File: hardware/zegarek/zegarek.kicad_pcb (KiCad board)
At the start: 4 copper layers, 100 x 100 mm, 106 parts, among them J1 Barrel_Jack_MountingPin, J2 Conn_01x02, J3 Conn_01x02, J4 Conn_01x04, M1 74141DIP16, M2 74141DIP16, M3 74141DIP16, M4 74141DIP16, Q1 IRF740, SW1 SW_Push, SW2 SW_Push, SW3 SW_Push, SW4 SW_Push, U1 DI78L3.3UAB, U2 MC34063AD, U3 L7805ACV, U4 STM32F091RCTx, U5 SN74LVC8T245, U6 SN74LVC8T245, Y1 32.768kHz

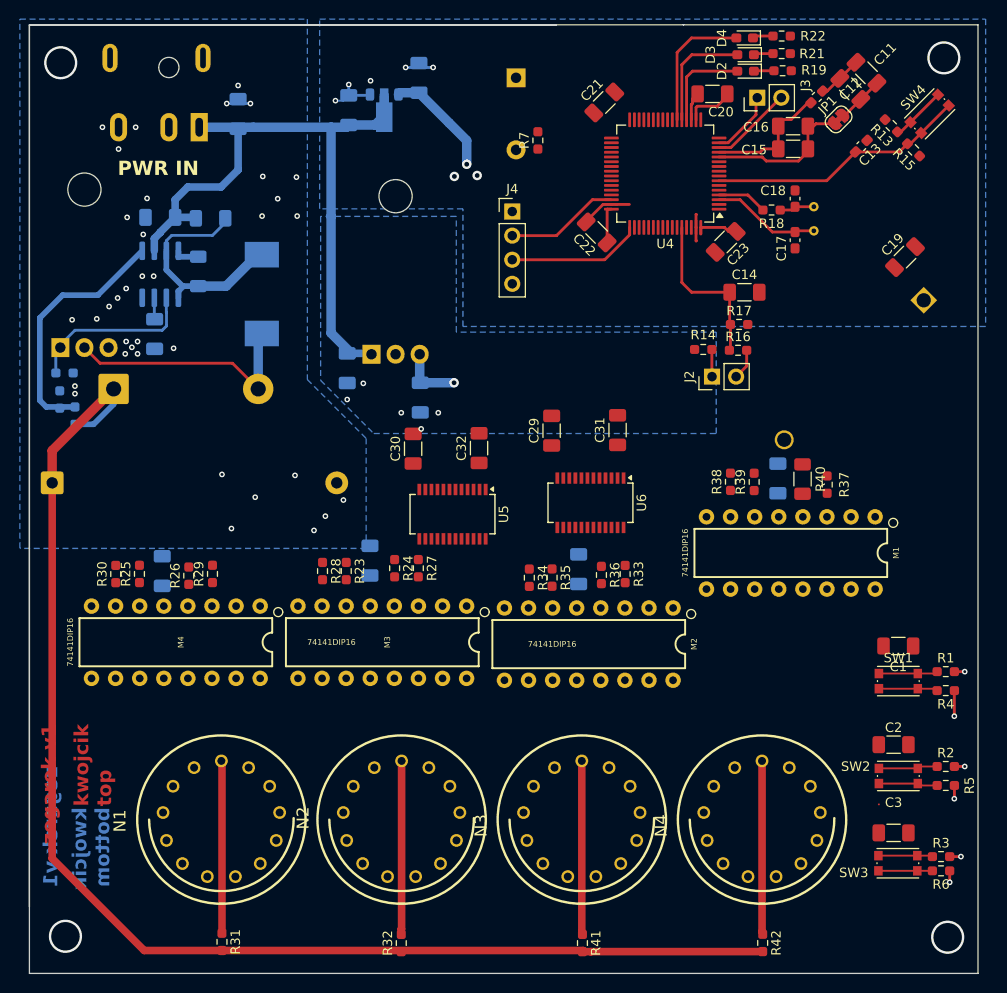
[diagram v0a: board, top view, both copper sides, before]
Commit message: tracing lamps
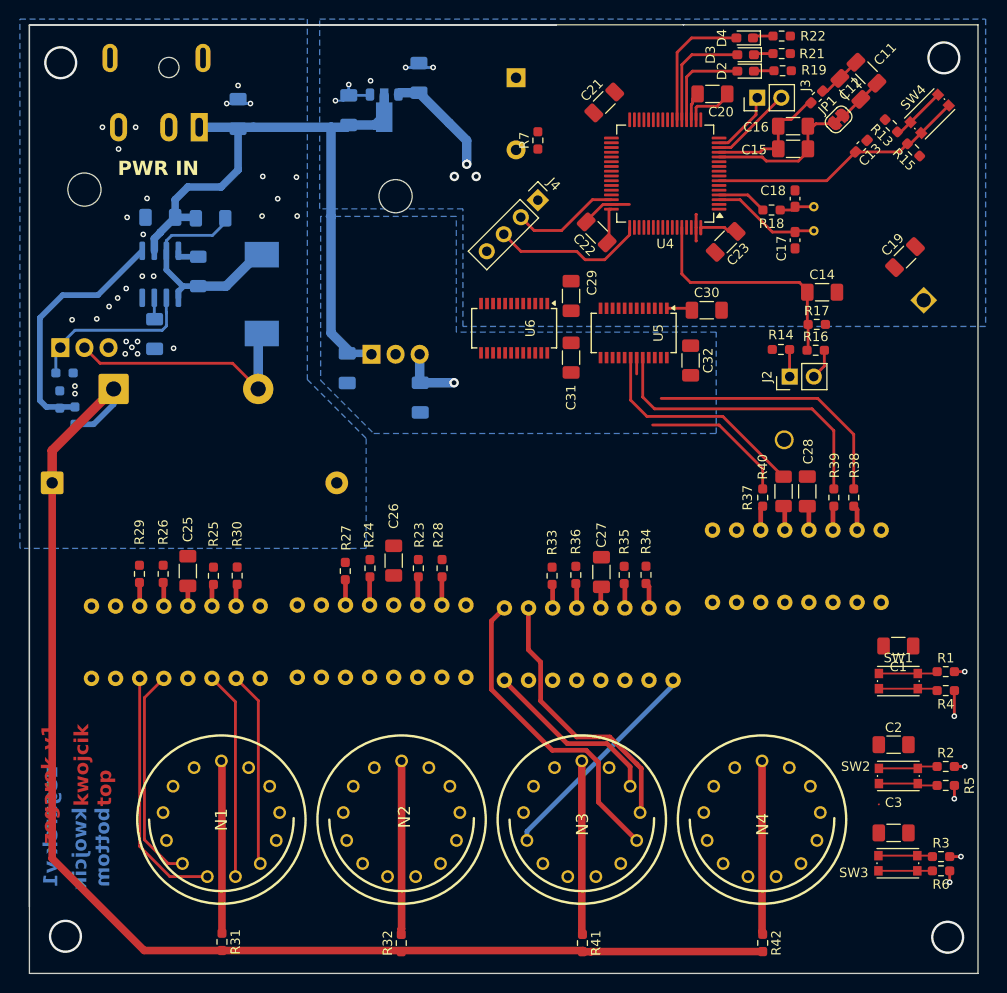
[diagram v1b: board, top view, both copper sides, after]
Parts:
- C25, C26, C27, C28: moved to F.Cu
- M1, M2, M3, M4: moved to B.Cu
- moved C30 34.2 mm to (116.4, 77.7), turned to 0 degrees
- moved U5 27.0 mm to (108.7, 80.1)
- moved C32 24.1 mm to (114.7, 83.0), turned to -90 degrees
- moved U6 20.1 mm to (96.1, 79.6)
- moved C29 14.3 mm to (102.1, 76.2)
- moved R38 13.1 mm to (131.9, 97.5)
- moved R30 12.8 mm to (66.9, 105.7)
- moved R28 12.6 mm to (88.5, 104.9)
- moved R34 12.3 mm to (110.0, 105.6)
- moved C31 9.07 mm to (102.1, 82.7), turned to -90 degrees
- moved R39 8.56 mm to (129.8, 97.5)
- moved C14 8.19 mm to (128.6, 75.8)
- moved J2 8.19 mm to (125.1, 84.7)
- moved R14 8.19 mm to (124.2, 81.8)
- moved R16 8.19 mm to (127.9, 81.9)
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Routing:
- net Net-(M2-2): track 0.00 -> 36.0 mm
- net Net-(M2-8): track 0.00 -> 33.5 mm
- net /NIXIE/5VHL_B: track 0.00 -> 31.9 mm
- net /NIXIE/5VHL_C: track 0.00 -> 29.3 mm
- net Net-(M2-9): track 0.00 -> 28.8 mm
- net Net-(M4-5): track 0.00 -> 26.2 mm
- net Net-(M2-4): track 0.00 -> 24.7 mm
- net /NIXIE/5VHL_D: track 0.00 -> 23.9 mm
- net Net-(M2-3): track 0.00 -> 23.3 mm
- net Net-(M4-4): track 0.00 -> 22.9 mm
- net Net-(M2-6): track 0.00 -> 22.2 mm
- net Net-(M4-6): track 0.00 -> 21.9 mm
- net Net-(M2-5): track 0.00 -> 21.4 mm
- net Net-(M4-7): track 0.00 -> 20.6 mm
- net Net-(M2-7): track 0.00 -> 20.6 mm
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
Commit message: tracing pcb
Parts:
- M3: value 74141DIP16 -> 74441DIP16
- moved C1 7.20 mm to (139.9, 119.5), turned to -90 degrees
- moved J4 5.60 mm to (93.0, 66.1), turned to 0 degrees
- moved C13 4.49 mm to (130.3, 64.2), turned to -45 degrees
- moved R1 2.39 mm to (139.3, 115.1), turned to 90 degrees
- moved C28 1.50 mm to (128.5, 96.8)
- moved M1 1.50 mm to (127.4, 104.7)
- moved R37 1.50 mm to (123.8, 97.5)
- moved R38 1.50 mm to (133.4, 97.5)
- moved R39 1.50 mm to (131.3, 97.5)
- moved R40 1.50 mm to (126.0, 96.8)
- moved R4 1.19 mm to (142.8, 117.8)
- moved SW1 1.10 mm to (135.5, 116.8)
- turned C6 to -90 degrees
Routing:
- net +3V3: track 76.1 -> 253.4 mm, vias 6 -> 13
- net +5V: track 13.7 -> 180.5 mm, vias 1 -> 3
- net /MCU/BTNDN: track 5.74 -> 115.6 mm, vias 0 -> 2
- net /MCU/BTNUP: track 6.24 -> 102.5 mm, vias 0 -> 2
- net /MCU/BTNOK: track 6.49 -> 78.0 mm, vias 0 -> 2
- net /NIXIE/5VHH_A: track 0.00 -> 58.9 mm, vias 0 -> 2
- net /MCU/HH_B: track 0.00 -> 55.0 mm, vias 0 -> 2
- net /NIXIE/5VHH_D: track 0.00 -> 54.3 mm, vias 0 -> 2
- net /MCU/HH_C: track 0.00 -> 51.6 mm, vias 0 -> 2
- net /MCU/HH_A: track 0.00 -> 51.5 mm, vias 0 -> 2
- net /NIXIE/5VHH_B: track 0.00 -> 50.8 mm, vias 0 -> 2
- net /NIXIE/5VHH_C: track 0.00 -> 48.0 mm, vias 0 -> 2
- net Net-(M1-3): track 0.00 -> 45.8 mm
- net Net-(M4-8): track 0.00 -> 45.2 mm
- net Net-(M1-2): track 0.00 -> 44.6 mm
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- added copper zone on F.Cu, net GND
- added copper zone on In2.Cu, net GND
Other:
- outline, holes or cut-outs redrawn
- board text added: "top kwojcik"
- board text removed: "kwojcik top"

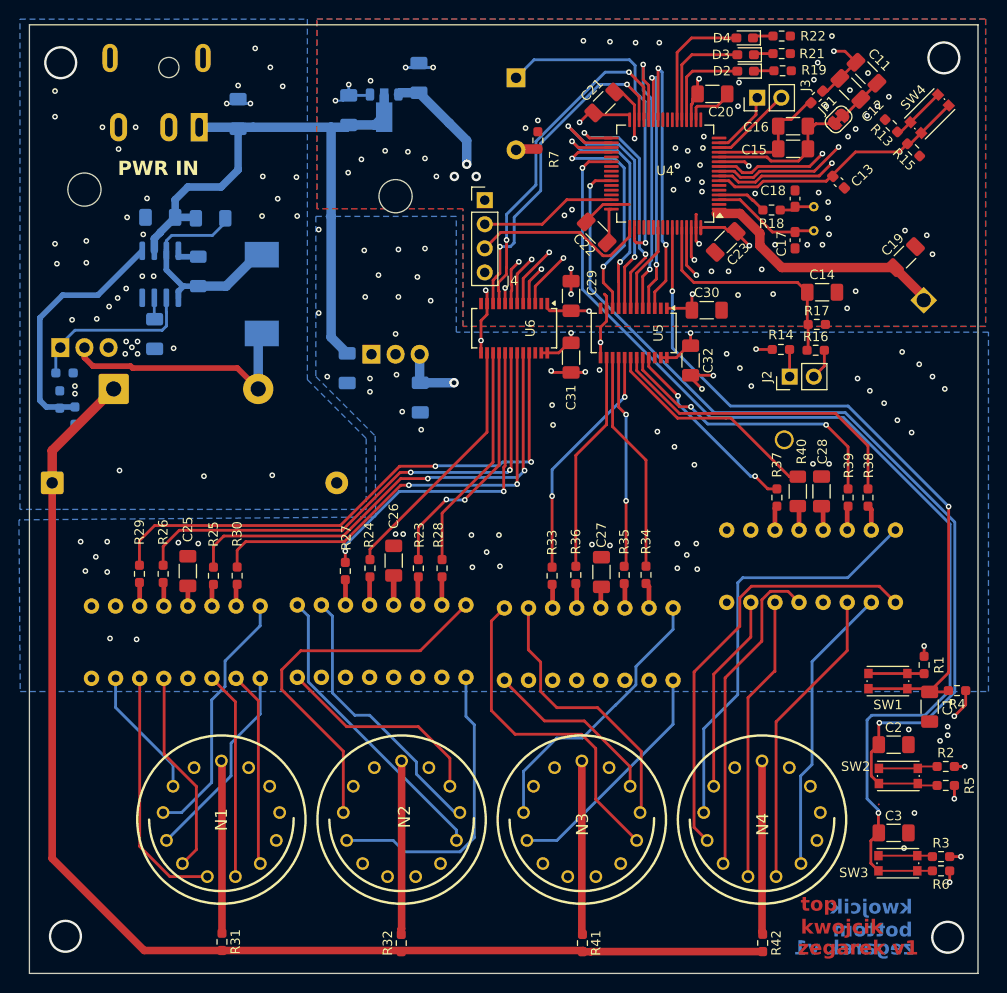
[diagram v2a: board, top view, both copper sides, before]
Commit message: changed dc connector footprint, DRCfixes done
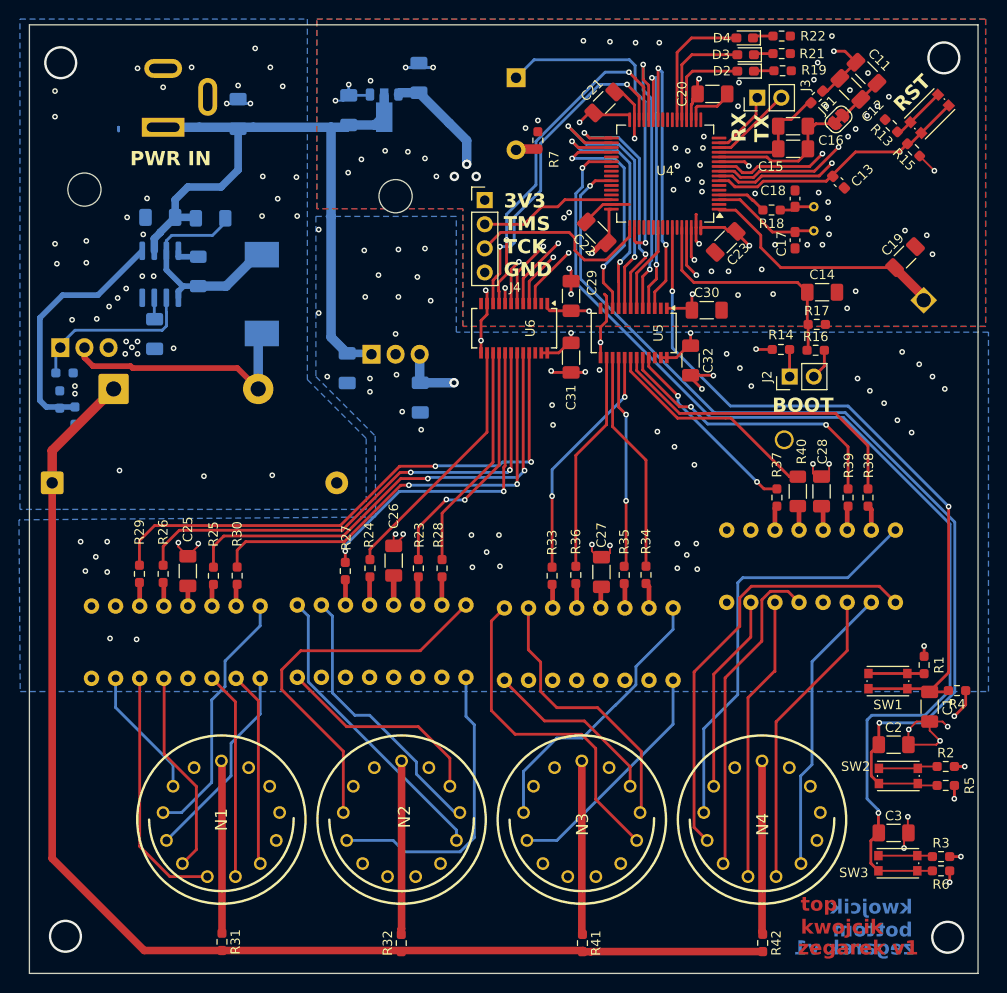
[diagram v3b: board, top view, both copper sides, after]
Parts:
- J1: footprint Connector_BarrelJack:BarrelJack_CUI_PJ-079BH_Horizontal -> Connector_BarrelJack:BarrelJack_Kycon_KLDX-0202-xC_Horizontal
- M3: value 74441DIP16 -> 74141DIP16
- moved J1 3.80 mm to (59.1, 58.4), turned to -90 degrees
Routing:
- net +3V3: track 253.4 -> 295.9 mm, vias 13 -> 15
- net GND: track 65.5 -> 95.9 mm, vias 175 -> 182
- net +12V: track 71.2 -> 77.5 mm
- net /MCU/TCK: track 18.8 -> 19.9 mm
- net /MCU/BTNUP: track 102.5 -> 103.3 mm
- net /MCU/BTNDN: track 115.6 -> 116.2 mm
- net (no net): vias 10 -> 2
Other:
- board text added: "3V3 TMS TCK GND"
- board text added: "BOOT"
- board text added: "RST"
- board text added: "RX TX"

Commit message: silk fixes
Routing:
- net +5V: track 180.5 -> 176.5 mm, vias 3 -> 5
- net /MCU/TMS: track 14.4 -> 18.1 mm
- net /MCU/TCK: track 19.9 -> 18.5 mm
- net GND: track 95.9 -> 97.3 mm, vias 182 -> 216
- net +3V3: track 295.9 -> 297.1 mm
- net /MCU/HH_C: track 51.6 -> 52.7 mm
- net /NIXIE/5VMH_B: track 26.5 -> 27.2 mm
- net /MCU/MH_D: track 35.5 -> 35.0 mm

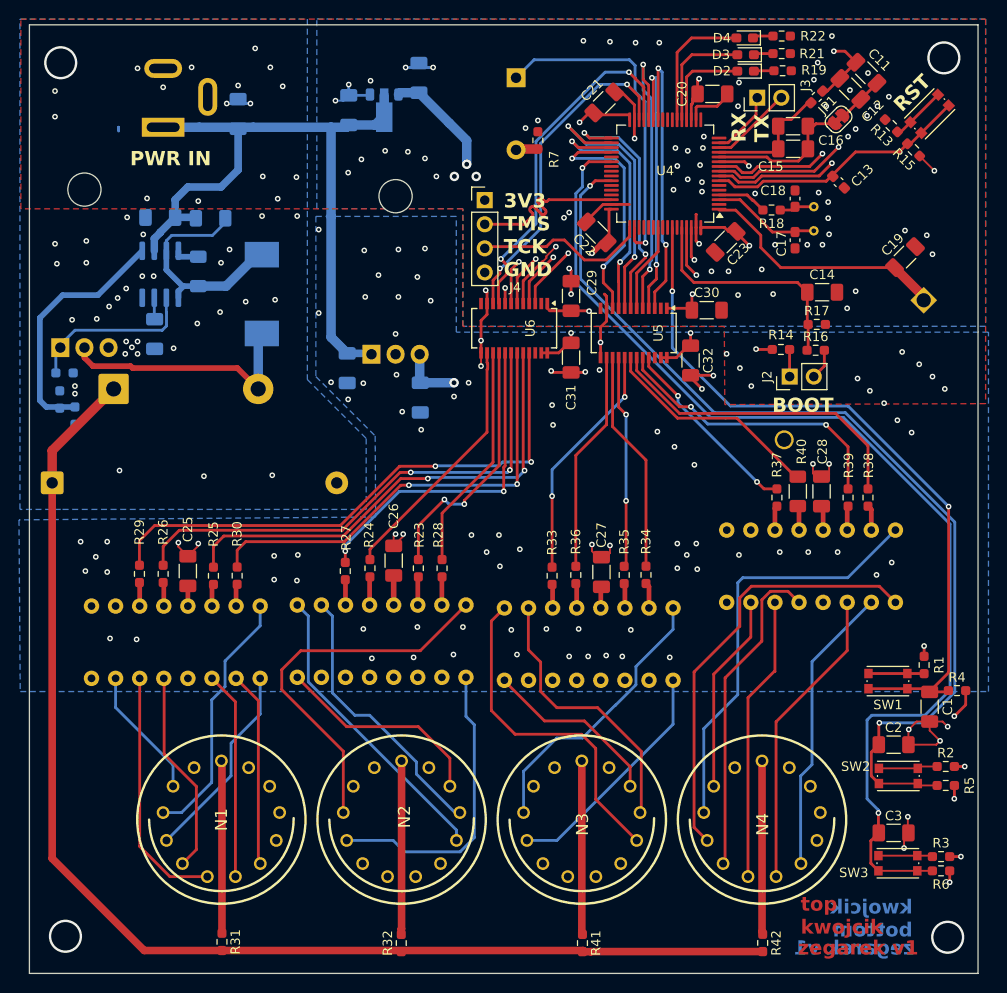
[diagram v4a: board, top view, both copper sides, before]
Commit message: rerouting tubes order for proper display order
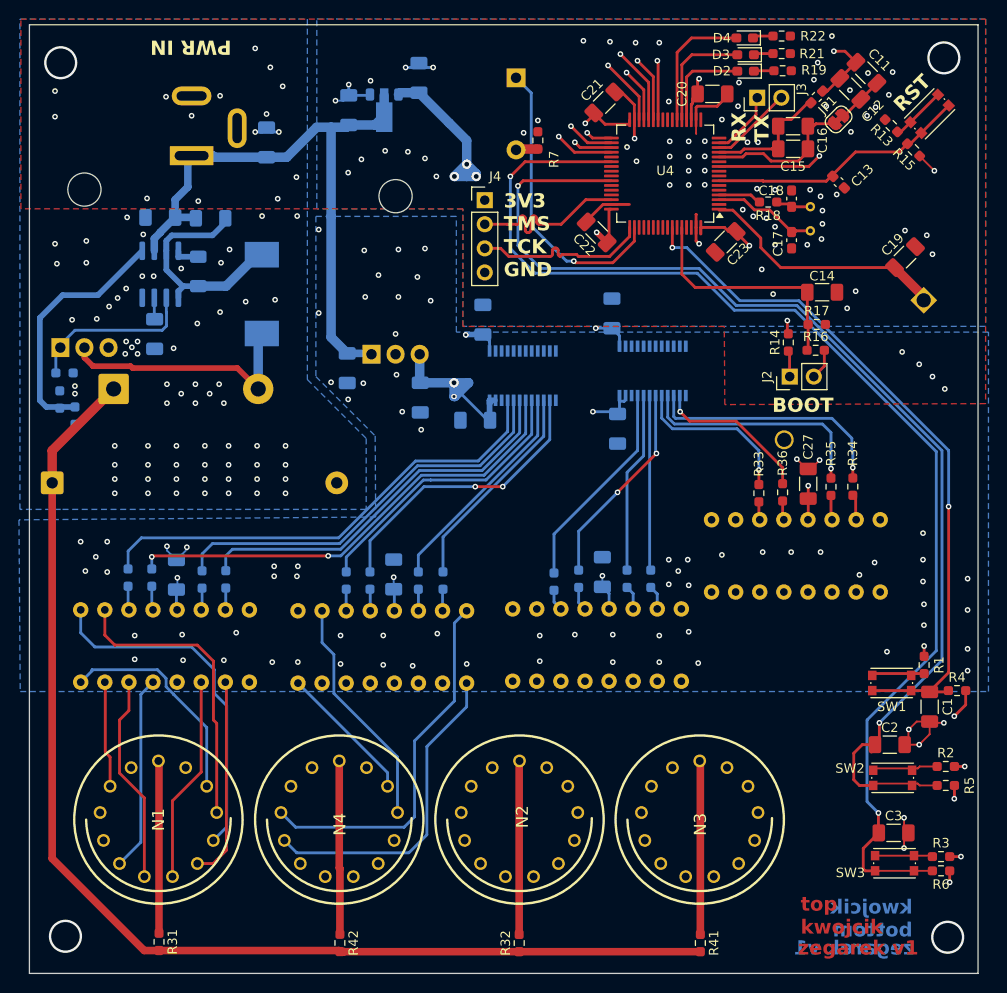
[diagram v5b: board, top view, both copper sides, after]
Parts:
- C25, C26, C28, C29, C30, C31, C32, R23, R24, R25, R26, R27, R28, R29, R30, R37, R38, R39, U5, U6: moved to B.Cu
- J1: footprint Connector_BarrelJack:BarrelJack_Kycon_KLDX-0202-xC_Horizontal -> Connector_BarrelJack:BarrelJack_GCT_DCJ200-10-A_Horizontal
- R40: footprint Resistor_SMD:R_1206_3216Metric_Pad1.30x1.75mm_HandSolder -> Resistor_SMD:R_0603_1608Metric_Pad0.98x0.95mm_HandSolder; moved to B.Cu
- moved R37 46.2 mm to (78.4, 106.2)
- moved R39 46.1 mm to (86.0, 106.2)
- moved R40 46.1 mm to (80.9, 106.2)
- moved M1 46.0 mm to (82.2, 113.2)
- moved C28 45.9 mm to (83.4, 105.5)
- moved R38 45.6 mm to (88.6, 106.2)
- moved R42 44.6 mm to (77.7, 144.4)
- moved N4 44.6 mm to (77.7, 131.4)
- moved M2 23.7 mm to (125.8, 103.6)
- moved R34 23.7 mm to (131.8, 96.3)
- moved C27 23.7 mm to (127.1, 96.0)
- moved R35 23.7 mm to (129.5, 96.3)
- moved R33 23.5 mm to (121.9, 97.0)
- moved R36 23.5 mm to (124.4, 96.9)
- moved M3 22.7 mm to (104.8, 113.0)
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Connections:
- U5 pad 10: /MCU/ML_D -> /MCU/HL_D
- U5 pad 14: /NIXIE/5VML_D -> /NIXIE/5VHL_D
- U5 pad 15: /NIXIE/5VML_C -> /NIXIE/5VHL_C
- U5 pad 16: /NIXIE/5VML_B -> /NIXIE/5VHL_B
- U5 pad 17: /NIXIE/5VML_A -> /NIXIE/5VHL_A
- U5 pad 18: /NIXIE/5VHL_D -> /NIXIE/5VHH_D
- U5 pad 19: /NIXIE/5VHL_C -> /NIXIE/5VHH_C
- U5 pad 20: /NIXIE/5VHL_B -> /NIXIE/5VHH_B
- U5 pad 21: /NIXIE/5VHL_A -> /NIXIE/5VHH_A
- U5 pad 3: /MCU/HL_A -> /MCU/HH_A
- U5 pad 4: /MCU/HL_B -> /MCU/HH_B
- U5 pad 5: /MCU/HL_C -> /MCU/HH_C
- U5 pad 6: /MCU/HL_D -> /MCU/HH_D
- U5 pad 7: /MCU/ML_A -> /MCU/HL_A
- U5 pad 8: /MCU/ML_B -> /MCU/HL_B
- U5 pad 9: /MCU/ML_C -> /MCU/HL_C
- U6 pad 10: /MCU/MH_D -> /MCU/ML_D
- U6 pad 14: /NIXIE/5VMH_D -> /NIXIE/5VML_D
- U6 pad 15: /NIXIE/5VMH_C -> /NIXIE/5VML_C
- U6 pad 16: /NIXIE/5VMH_B -> /NIXIE/5VML_B
- U6 pad 17: /NIXIE/5VMH_A -> /NIXIE/5VML_A
- U6 pad 18: /NIXIE/5VHH_D -> /NIXIE/5VMH_D
- U6 pad 19: /NIXIE/5VHH_C -> /NIXIE/5VMH_C
- U6 pad 20: /NIXIE/5VHH_B -> /NIXIE/5VMH_B
- U6 pad 21: /NIXIE/5VHH_A -> /NIXIE/5VMH_A
- U6 pad 3: /MCU/HH_A -> /MCU/MH_A
- U6 pad 4: /MCU/HH_B -> /MCU/MH_B
- U6 pad 5: /MCU/HH_C -> /MCU/MH_C
- U6 pad 6: /MCU/HH_D -> /MCU/MH_D
- U6 pad 7: /MCU/MH_A -> /MCU/ML_A
- U6 pad 8: /MCU/MH_B -> /MCU/ML_B
- U6 pad 9: /MCU/MH_C -> /MCU/ML_C
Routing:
- net /MCU/HH_B: track 55.0 -> 0.00 mm, vias 2 -> 0
- net /MCU/HH_A: track 51.5 -> 0.00 mm, vias 2 -> 0
- net /MCU/HH_C: track 52.7 -> 12.1 mm, vias 2 -> 1
- net Net-(M3-2): track 40.0 -> 0.00 mm
- net GND: track 97.3 -> 61.6 mm, vias 216 -> 240
- net /MCU/HH_D: track 35.6 -> 0.00 mm, vias 2 -> 0
- net Net-(M2-8): track 35.5 -> 0.00 mm
- net /MCU/MH_C: track 37.7 -> 5.73 mm, vias 2 -> 1
- net Net-(M3-3): track 31.8 -> 0.00 mm
- net Net-(M3-8): track 31.8 -> 0.00 mm
- net Net-(M2-2): track 29.7 -> 0.00 mm
- net /MCU/MH_A: track 29.6 -> 0.00 mm, vias 2 -> 0
- net Net-(M2-9): track 29.3 -> 0.00 mm
- net Net-(M3-9): track 29.1 -> 0.00 mm
- net /MCU/MH_B: track 29.0 -> 0.00 mm, vias 2 -> 0
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
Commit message: correction changes, postprod files regenration,added OE and EN to MCU schematic
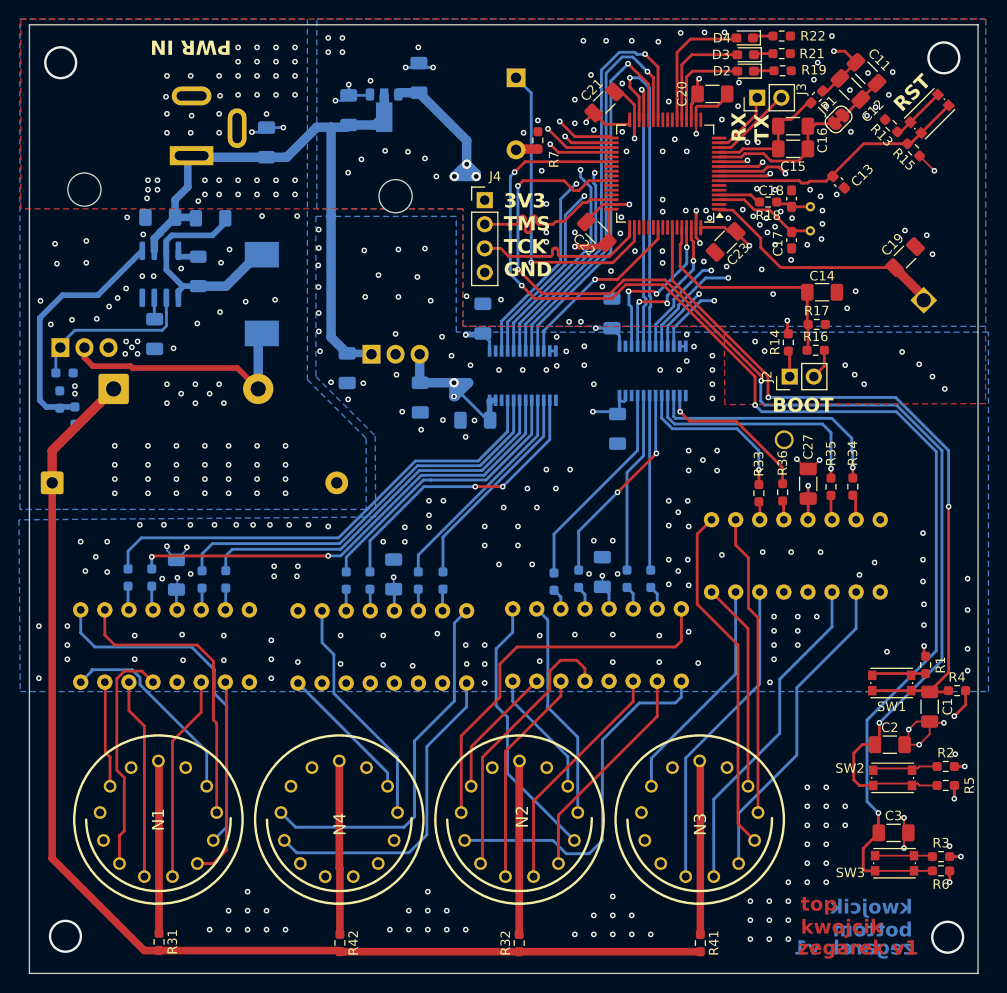
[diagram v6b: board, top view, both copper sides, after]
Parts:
- moved R1 0.16 mm to (139.5, 115.1)
- moved C29 0.11 mm to (92.8, 78.6)
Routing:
- net /MCU/HH_B: track 0.00 -> 49.4 mm, vias 0 -> 2
- net Net-(M2-2): track 0.00 -> 47.5 mm
- net /MCU/HH_A: track 0.00 -> 47.4 mm, vias 0 -> 2
- net Net-(M2-3): track 0.00 -> 45.5 mm
- net /MCU/HH_D: track 0.00 -> 41.9 mm, vias 0 -> 2
- net /MCU/ML_A: track 2.78 -> 43.9 mm, vias 1 -> 2
- net Net-(M3-2): track 0.00 -> 40.9 mm
- net /MCU/HL_A: track 6.26 -> 45.9 mm
- net /MCU/ML_B: track 4.99 -> 44.2 mm, vias 1 -> 2
- net Net-(M3-3): track 0.00 -> 38.1 mm
- net /MCU/ML_C: track 4.08 -> 41.2 mm, vias 1 -> 2
- net Net-(M2-8): track 0.00 -> 36.9 mm
- net /MCU/HL_B: track 6.92 -> 43.6 mm
- net /MCU/HH_C: track 12.1 -> 48.1 mm, vias 1 -> 2
- net /MCU/ML_D: track 6.23 -> 41.6 mm, vias 1 -> 2
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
